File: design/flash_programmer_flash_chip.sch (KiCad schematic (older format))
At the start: 12 parts

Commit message: Work in progress: Come up with untested A9_P circuit
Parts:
- added Q? (x3): 2N3904, symbol Q_NPN_BCE
- added R? (x2): 1k, Resistors_SMD:R_0805_HandSoldering, symbol R
- added R?: 10k, Resistors_SMD:R_0805_HandSoldering, symbol R
- R?: value 10k -> 1k
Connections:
- wire segments 67 -> 80
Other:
- note added: "Logical NOT on the STU line"
- note added: "TODO: Test this A9_P circuit"
- note removed: "TODO: VPP needs to be disconnected somehow when not in write mode"
- moved on the sheet: D?, R?
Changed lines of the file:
@@
 Text Label 1400 1700 1    60   ~ 0
 A[0..16]
-Text Label 7150 4750 1    60   ~ 0
+Text Label 8150 6150 2    60   ~ 0
 A[0..16]
 Wire Wire Line
@@
 L GND #PWR?
 U 1 1 58BA7CFB
-P 9800 3050
-F 0 "#PWR?" H 9800 2800 50  0001 C CNN
-F 1 "GND" H 9800 2900 50  0000 C CNN
-F 2 "" H 9800 3050 50  0000 C CNN
-F 3 "" H 9800 3050 50  0000 C CNN
-	1    9800 3050
-	0    -1   -1   0
+P 6900 5500
+F 0 "#PWR?" H 6900 5250 50  0001 C CNN
+F 1 "GND" H 6900 5350 50  0000 C CNN
+F 2 "" H 6900 5500 50  0000 C CNN
+F 3 "" H 6900 5500 50  0000 C CNN
+	1    6900 5500
+	1    0    0    -1
 $EndComp
 $Comp
@@
 L R R?
 U 1 1 58BA7EA3
-P 3050 6200
-F 0 "R?" V 3130 6200 50  0000 C CNN
-F 1 "10k" V 3050 6200 50  0000 C CNN
-F 2 "Resistors_SMD:R_0805_HandSoldering" V 2980 6200 50  0001 C CNN
-F 3 "" H 3050 6200 50  0000 C CNN
-	1    3050 6200
-	-1   0    0    1
+P 6300 5200
+F 0 "R?" V 6380 5200 50  0000 C CNN
+F 1 "1k" V 6300 5200 50  0000 C CNN
+F 2 "Resistors_SMD:R_0805_HandSoldering" V 6230 5200 50  0001 C CNN
+F 3 "" H 6300 5200 50  0000 C CNN
+	1    6300 5200
+	0    -1   -1   0
 $EndComp
 Wire Wire Line
@@
 L D_Schottky D?
 U 1 1 58BAFC52
-P 6400 5050
-F 0 "D?" H 6400 5150 50  0000 C CNN
-F 1 "BAT54" H 6400 4950 50  0000 C CNN
-F 2 "" H 6400 5050 50  0000 C CNN
-F 3 "" H 6400 5050 50  0000 C CNN
-	1    6400 5050
-	1    0    0    -1
+P 7750 5400
+F 0 "D?" H 7750 5500 50  0000 C CNN
+F 1 "BAT54" H 7750 5300 50  0000 C CNN
+F 2 "" H 7750 5400 50  0000 C CNN
+F 3 "" H 7750 5400 50  0000 C CNN
+	1    7750 5400
+	0    1    1    0
 $EndComp
 Wire Bus Line
-	7150 5050 7150 4350
-Wire Wire Line
-	7150 5050 6550 5050
-Text Label 6750 5050 0    60   ~ 0
+	8450 6150 7750 6150
+Wire Wire Line
+	7750 5550 7750 6150
+Text Label 7750 5950 1    60   ~ 0
 A9
-Wire Wire Line
-	5400 5050 6250 5050
-Wire Wire Line
-	7150 5350 5900 5350
-Text Label 6750 5350 0    60   ~ 0
-VPP
-Wire Wire Line
-	5900 5350 5900 5050
-Connection ~ 5900 5050
-Text Label 5500 5050 0    60   ~ 0
-A9_P
 Wire Wire Line
 	3050 2400 3450 2400
 Text Label 3150 2400 0    60   ~ 0
 A9_P
-Text Notes 5150 5550 0    60   ~ 0
-TODO: VPP needs to be disconnected somehow when not in write mode
 Wire Wire Line
 	5100 7600 6350 7600
@@
 Text Label 5250 7600 0    60   ~ 0
 STU
+$Comp
+L Q_NPN_BCE Q?
+U 1 1 58BEF822
+P 6800 5200
+F 0 "Q?" H 7000 5250 50  0000 L CNN
+F 1 "2N3904" H 7000 5150 50  0000 L CNN
+F 2 "" H 7000 5300 50  0000 C CNN
+F 3 "" H 6800 5200 50  0000 C CNN
+	1    6800 5200
+	1    0    0    -1
+$EndComp
+Wire Wire Line
+	7750 4850 7750 5250
+Wire Wire Line
+	7750 5000 8300 5000
+Text Label 8100 5000 0    60   ~ 0
+A9_P
+Wire Wire Line
+	7350 4650 7450 4650
+Wire Wire Line
+	7050 4650 6900 4650
+Wire Wire Line
+	6900 4200 6900 5000
+Wire Wire Line
+	6900 4200 7750 4200
+Wire Wire Line
+	7750 4200 7750 4450
+Text Label 7300 4000 1    60   ~ 0
+VPP
+Wire Wire Line
+	7300 4200 7300 3800
+Connection ~ 7300 4200
+Connection ~ 6900 4650
+Wire Wire Line
+	6900 5400 6900 5500
+$Comp
+L Q_NPN_BCE Q?
+U 1 1 58BF03A4
+P 7650 4650
+F 0 "Q?" H 7850 4700 50  0000 L CNN
+F 1 "2N3904" H 7850 4600 50  0000 L CNN
+F 2 "" H 7850 4750 50  0000 C CNN
+F 3 "" H 7650 4650 50  0000 C CNN
+	1    7650 4650
+	1    0    0    -1
+$EndComp
+$Comp
+L R R?
+U 1 1 58BF0471
+P 7200 4650
+F 0 "R?" V 7280 4650 50  0000 C CNN
+F 1 "1k" V 7200 4650 50  0000 C CNN
+F 2 "Resistors_SMD:R_0805_HandSoldering" V 7130 4650 50  0001 C CNN
+F 3 "" H 7200 4650 50  0000 C CNN
+	1    7200 4650
+	0    -1   -1   0
+$EndComp
+Wire Wire Line
+	6450 5200 6600 5200
+$Comp
+L Q_NPN_BCE Q?
+U 1 1 58BF0576
+P 5750 5500
+F 0 "Q?" H 5950 5550 50  0000 L CNN
+F 1 "2N3904" H 5950 5450 50  0000 L CNN
+F 2 "" H 5950 5600 50  0000 C CNN
+F 3 "" H 5750 5500 50  0000 C CNN
+	1    5750 5500
+	1    0    0    -1
+$EndComp
+$Comp
+L GND #PWR?
+U 1 1 58BF059E
+P 5850 5800
+F 0 "#PWR?" H 5850 5550 50  0001 C CNN
+F 1 "GND" H 5850 5650 50  0000 C CNN
+F 2 "" H 5850 5800 50  0000 C CNN
+F 3 "" H 5850 5800 50  0000 C CNN
+	1    5850 5800
+	1    0    0    -1
+$EndComp
+Wire Wire Line
+	5850 5050 5850 5300
+Wire Wire Line
+	5850 5200 6150 5200
+Wire Wire Line
+	5850 5700 5850 5800
+$Comp
+L R R?
+U 1 1 58BF0846
+P 5850 4900
+F 0 "R?" V 5930 4900 50  0000 C CNN
+F 1 "10k" V 5850 4900 50  0000 C CNN
+F 2 "Resistors_SMD:R_0805_HandSoldering" V 5780 4900 50  0001 C CNN
+F 3 "" H 5850 4900 50  0000 C CNN
+	1    5850 4900
+	1    0    0    -1
+$EndComp
+Connection ~ 5850 5200
+$Comp
+L VCC #PWR?
+U 1 1 58BF0A83
+P 5850 4600
+F 0 "#PWR?" H 5850 4450 50  0001 C CNN
+F 1 "VCC" H 5850 4750 50  0000 C CNN
+F 2 "" H 5850 4600 50  0000 C CNN
+F 3 "" H 5850 4600 50  0000 C CNN
+	1    5850 4600
+	1    0    0    -1
+$EndComp
+Wire Wire Line
+	5850 4600 5850 4750
+Wire Wire Line
+	5550 5500 5350 5500
+$Comp
+L R R?
+U 1 1 58BF0CDC
+P 5200 5500
+F 0 "R?" V 5280 5500 50  0000 C CNN
+F 1 "1k" V 5200 5500 50  0000 C CNN
+F 2 "Resistors_SMD:R_0805_HandSoldering" V 5130 5500 50  0001 C CNN
+F 3 "" H 5200 5500 50  0000 C CNN
+	1    5200 5500
+	0    -1   -1   0
+$EndComp
+Wire Wire Line
+	5050 5500 4750 5500
+Text Label 4750 5500 0    60   ~ 0
+STU
+Wire Notes Line
+	5000 4200 5000 6150
+Wire Notes Line
+	5000 6150 6100 6150
+Wire Notes Line
+	6100 6150 6100 4200
+Wire Notes Line
+	6100 4200 5000 4200
+Text Notes 4900 4150 0    60   ~ 0
+Logical NOT on the STU line
+Connection ~ 7750 5000
+Text Notes 5600 3700 0    60   ~ 0
+TODO: Test this A9_P circuit
 $EndSCHEMATC

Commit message: Redo the A9_P circuit with a P-channel MOSFET to avoid voltage drop
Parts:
- removed D?: BAT54, symbol D_Schottky
- removed Q? (x3): 2N3904, symbol Q_NPN_BCE
- removed R? (x3): 1k, Resistors_SMD:R_0805_HandSoldering, symbol R
- removed R?: 10k, Resistors_SMD:R_0805_HandSoldering, symbol R
- added D302: BAT54, symbol D_Schottky
- added Q301: 2N3904, symbol Q_NPN_BCE
- added Q302: BSS84, symbol Q_PMOS_DGS
- added R302, R303: 4.7k, Resistors_SMD:R_0805_HandSoldering, symbol R
- added R304: 10k, Resistors_SMD:R_0805_HandSoldering, symbol R
- gave numbers to parts that had none: 10
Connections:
- wire segments 80 -> 77
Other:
- note added: "Circuit to switch between VPP and A9 on the A9 pin of the GLS27SF010.\nWhen STU is HIGH, then VPP is 5V, the P-Channel MOSFET shuts off,\nand the PNP Transistor turns on which pulls A9_P to ground (since the diode\nis preventing current from flowing in that direction)."
- note removed: "Logical NOT on the STU line"
- note removed: "TODO: Test this A9_P circuit"

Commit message: Redraw schematic for clarity
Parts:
- removed D301: LED, LEDs:LED_0805, symbol LED
- removed R301: 150, Resistors_SMD:R_0805_HandSoldering, symbol R
- removed R302: 4.7k, Resistors_SMD:R_0805_HandSoldering, symbol R
- removed U301: GLS27SF010, Housings_DIP:DIP-32_W15.24mm, symbol GLS27SF010
- removed U302: 2N3906, TO_SOT_Packages_SMD:SOT-23_Handsoldering, symbol 2N3906
- added U401: GLS27SF010, symbol GLS27SF010
- C401: renamed from C301; value 120nF -> 100nF
- renumbered C305 to C402, C302 to C403, C303 to C404, C304 to C405, D302 to D401, Q302 to Q401, Q301 to Q402, R304 to R401, R303 to R402, U303 to U402
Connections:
- net labels added: CE_L, OE_L, PGM_L
- net labels removed: CE#, OE#, PGM#
- wire segments 77 -> 67
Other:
- note added: "Bypass capacitor for GLS27SF010"
- note added: "Bypass capacitor for MAX662A"
- note removed: "Bypass capacitors for GLS27SF010"
- note removed: "Bypass capacitors for MAX662A"
- note removed: "Write indicator light"
- moved on the sheet: C401, C402, C403, C404, C405, D401, Q402, R401, R402, U402

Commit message: Associate footprints and correct pin orders for transistors
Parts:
- removed Q401: BSS84, symbol Q_PMOS_DGS
- removed Q402: 2N3904, symbol Q_NPN_BCE
- added Q401: BSS84P, TO_SOT_Packages_SMD:SOT-23_Handsoldering, symbol Q_PMOS_GSD
- added Q402: 2N3904, symbol Q_NPN_BEC
- D401: footprint (none) -> Diodes_SMD:D_SOT-23_ANK
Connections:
- wire segments 67 -> 73
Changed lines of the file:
@@
 $EndComp
 $Comp
-L GND #PWR041
+L GND #PWR404
 U 1 1 58BA7A65
 P 6100 7200
-F 0 "#PWR041" H 6100 6950 50  0001 C CNN
+F 0 "#PWR404" H 6100 6950 50  0001 C CNN
 F 1 "GND" H 6100 7050 50  0000 C CNN
 F 2 "" H 6100 7200 50  0000 C CNN
@@
 $EndComp
 $Comp
-L VCC #PWR042
+L VCC #PWR403
 U 1 1 58BA7A6B
 P 6100 6600
-F 0 "#PWR042" H 6100 6450 50  0001 C CNN
+F 0 "#PWR403" H 6100 6450 50  0001 C CNN
 F 1 "VCC" H 6100 6750 50  0000 C CNN
 F 2 "" H 6100 6600 50  0000 C CNN
@@
 	2550 6450 2750 6450
 $Comp
-L VCC #PWR043
+L VCC #PWR402
 U 1 1 58BA7A7D
 P 2800 5900
-F 0 "#PWR043" H 2800 5750 50  0001 C CNN
+F 0 "#PWR402" H 2800 5750 50  0001 C CNN
 F 1 "VCC" H 2800 6050 50  0000 C CNN
 F 2 "" H 2800 5900 50  0000 C CNN
@@
 $EndComp
 $Comp
-L GND #PWR044
+L GND #PWR401
 U 1 1 58BA7A83
 P 2550 5900
-F 0 "#PWR044" H 2550 5650 50  0001 C CNN
+F 0 "#PWR401" H 2550 5650 50  0001 C CNN
 F 1 "GND" H 2550 5750 50  0000 C CNN
 F 2 "" H 2550 5900 50  0000 C CNN
@@
 	9950 4500 9950 4650
 Wire Wire Line
-	7950 4850 9050 4850
-$Comp
-L GND #PWR045
+	7950 4850 8550 4850
+Wire Wire Line
+	8550 4850 9050 4850
+$Comp
+L GND #PWR407
 U 1 1 58BA7CE6
 P 8900 4750
-F 0 "#PWR045" H 8900 4500 50  0001 C CNN
+F 0 "#PWR407" H 8900 4500 50  0001 C CNN
 F 1 "GND" H 8900 4600 50  0000 C CNN
 F 2 "" H 8900 4750 50  0000 C CNN
@@
 $EndComp
 $Comp
-L VCC #PWR046
+L VCC #PWR408
 U 1 1 58BA7CEC
 P 8950 5100
-F 0 "#PWR046" H 8950 4950 50  0001 C CNN
+F 0 "#PWR408" H 8950 4950 50  0001 C CNN
 F 1 "VCC" H 8950 5250 50  0000 C CNN
 F 2 "" H 8950 5100 50  0000 C CNN
@@
 $EndComp
 $Comp
-L VCC #PWR047
+L VCC #PWR409
 U 1 1 58BA7D01
 P 10900 4500
-F 0 "#PWR047" H 10900 4350 50  0001 C CNN
+F 0 "#PWR409" H 10900 4350 50  0001 C CNN
 F 1 "VCC" H 10900 4650 50  0000 C CNN
 F 2 "" H 10900 4500 50  0000 C CNN
@@
 	8550 5300 8550 5400
 $Comp
-L GND #PWR048
+L GND #PWR406
 U 1 1 58BA7D27
 P 8550 5400
-F 0 "#PWR048" H 8550 5150 50  0001 C CNN
+F 0 "#PWR406" H 8550 5150 50  0001 C CNN
 F 1 "GND" H 8550 5250 50  0000 C CNN
 F 2 "" H 8550 5400 50  0000 C CNN
@@
 OE_L
 Wire Wire Line
-	7750 5150 6350 5150
-$Comp
-L Q_PMOS_DGS Q401
-U 1 1 58C18892
-P 6150 5150
-F 0 "Q401" H 6350 5200 50  0000 L CNN
-F 1 "BSS84" H 6350 5100 50  0000 L CNN
-F 2 "" H 6350 5250 50  0000 C CNN
-F 3 "" H 6150 5150 50  0000 C CNN
-	1    6150 5150
-	-1   0    0    -1
-$EndComp
-$Comp
-L Q_NPN_BCE Q402
-U 1 1 58C18984
-P 6750 4450
-F 0 "Q402" V 7000 4400 50  0000 L CNN
-F 1 "2N3904" V 6700 4550 50  0000 L CNN
-F 2 "" H 6950 4550 50  0000 C CNN
-F 3 "" H 6750 4450 50  0000 C CNN
-	1    6750 4450
-	0    -1   -1   0
-$EndComp
+	7750 5150 6750 5150
+Wire Wire Line
+	6750 5150 6350 5150
 $Comp
 L R R401
@@
 $EndComp
 Wire Wire Line
-	2100 4350 6150 4350
+	2100 4350 6050 4350
+Wire Wire Line
+	6050 4350 6150 4350
 Wire Wire Line
 	6550 4350 6450 4350
@@
 	6750 4750 6750 4650
 $Comp
-L GND #PWR049
+L GND #PWR405
 U 1 1 58C19559
 P 7050 4350
-F 0 "#PWR049" H 7050 4100 50  0001 C CNN
+F 0 "#PWR405" H 7050 4100 50  0001 C CNN
 F 1 "GND" H 7050 4200 50  0000 C CNN
 F 2 "" H 7050 4350 50  0000 C CNN
@@
 	6050 5350 6050 5550
 Wire Wire Line
-	2450 5550 7950 5550
+	2450 5550 6050 5550
+Wire Wire Line
+	6050 5550 7950 5550
 Text Label 6900 5550 0    60   ~ 0
 VPP
@@
 F 0 "D401" H 5200 3750 50  0000 C CNN
 F 1 "BAT54" H 5200 3550 50  0000 C CNN
-F 2 "" H 5200 3650 50  0000 C CNN
+F 2 "Diodes_SMD:D_SOT-23_ANK" H 5200 3650 50  0001 C CNN
 F 3 "" H 5200 3650 50  0000 C CNN
 	1    5200 3650
@@
 PGM_L
 $Comp
-L GND #PWR050
+L GND #PWR410
 U 1 1 58C1FD4A
 P 10900 5100
-F 0 "#PWR050" H 10900 4850 50  0001 C CNN
+F 0 "#PWR410" H 10900 4850 50  0001 C CNN
 F 1 "GND" H 10900 4950 50  0000 C CNN
 F 2 "" H 10900 5100 50  0000 C CNN
@@
 	8900 4750 9050 4750
 Wire Wire Line
-	7750 4400 7750 5150
+	7750 4400 7750 4650
+Wire Wire Line
+	7750 4650 7750 5150
 Connection ~ 7750 4650
 Wire Wire Line
@@
 	1500 2950 1250 2950
 Wire Bus Line
-	3050 1550 3050 3550
+	3050 1550 3050 1950
+Wire Bus Line
+	3050 1950 3050 2050
+Wire Bus Line
+	3050 2050 3050 2150
+Wire Bus Line
+	3050 2150 3050 2250
+Wire Bus Line
+	3050 2250 3050 2350
+Wire Bus Line
+	3050 2350 3050 2450
+Wire Bus Line
+	3050 2450 3050 2550
+Wire Bus Line
+	3050 2550 3050 2650
+Wire Bus Line
+	3050 2650 3050 2750
+Wire Bus Line
+	3050 2750 3050 2850
+Wire Bus Line
+	3050 2850 3050 2950
+Wire Bus Line
+	3050 2950 3050 3050
+Wire Bus Line
+	3050 3050 3050 3150
+Wire Bus Line
+	3050 3150 3050 3250
+Wire Bus Line
+	3050 3250 3050 3350
+Wire Bus Line
+	3050 3350 3050 3450
+Wire Bus Line
+	3050 3450 3050 3550
 Wire Bus Line
 	3050 1550 3150 1550
@@
 	2950 1950 3050 2050
 Wire Bus Line
-	1150 1550 1150 2850
+	1150 1550 1150 2150
+Wire Bus Line
+	1150 2150 1150 2250
+Wire Bus Line
+	1150 2250 1150 2350
+Wire Bus Line
+	1150 2350 1150 2450
+Wire Bus Line
+	1150 2450 1150 2550
+Wire Bus Line
+	1150 2550 1150 2650
+Wire Bus Line
+	1150 2650 1150 2750
+Wire Bus Line
+	1150 2750 1150 2850
 Wire Bus Line
 	1150 1550 1050 1550
@@
 	5350 3650 6050 3650
 Wire Wire Line
-	6050 3650 6050 4950
+	6050 3650 6050 4350
+Wire Wire Line
+	6050 4350 6050 4950
 Wire Wire Line
 	2100 4350 2100 3850
 Connection ~ 6050 5550
+$Comp
+L Q_PMOS_GSD Q401
+U 1 1 58C2CBBF
+P 6150 5150
+F 0 "Q401" H 6350 5200 50  0000 L CNN
+F 1 "BSS84P" H 6350 5100 50  0000 L CNN
+F 2 "TO_SOT_Packages_SMD:SOT-23_Handsoldering" H 6350 5250 50  0001 C CNN
+F 3 "" H 6150 5150 50  0000 C CNN
+	1    6150 5150
+	-1   0    0    -1
+$EndComp
+$Comp
+L Q_NPN_BEC Q402
+U 1 1 58C2EB64
+P 6750 4450
+F 0 "Q402" V 6700 4150 50  0000 L CNN
+F 1 "2N3904" V 6950 4300 50  0000 L CNN
+F 2 "" H 6950 4550 50  0000 C CNN
+F 3 "" H 6750 4450 50  0000 C CNN
+	1    6750 4450
+	0    -1   -1   0
+$EndComp
 $EndSCHEMATC

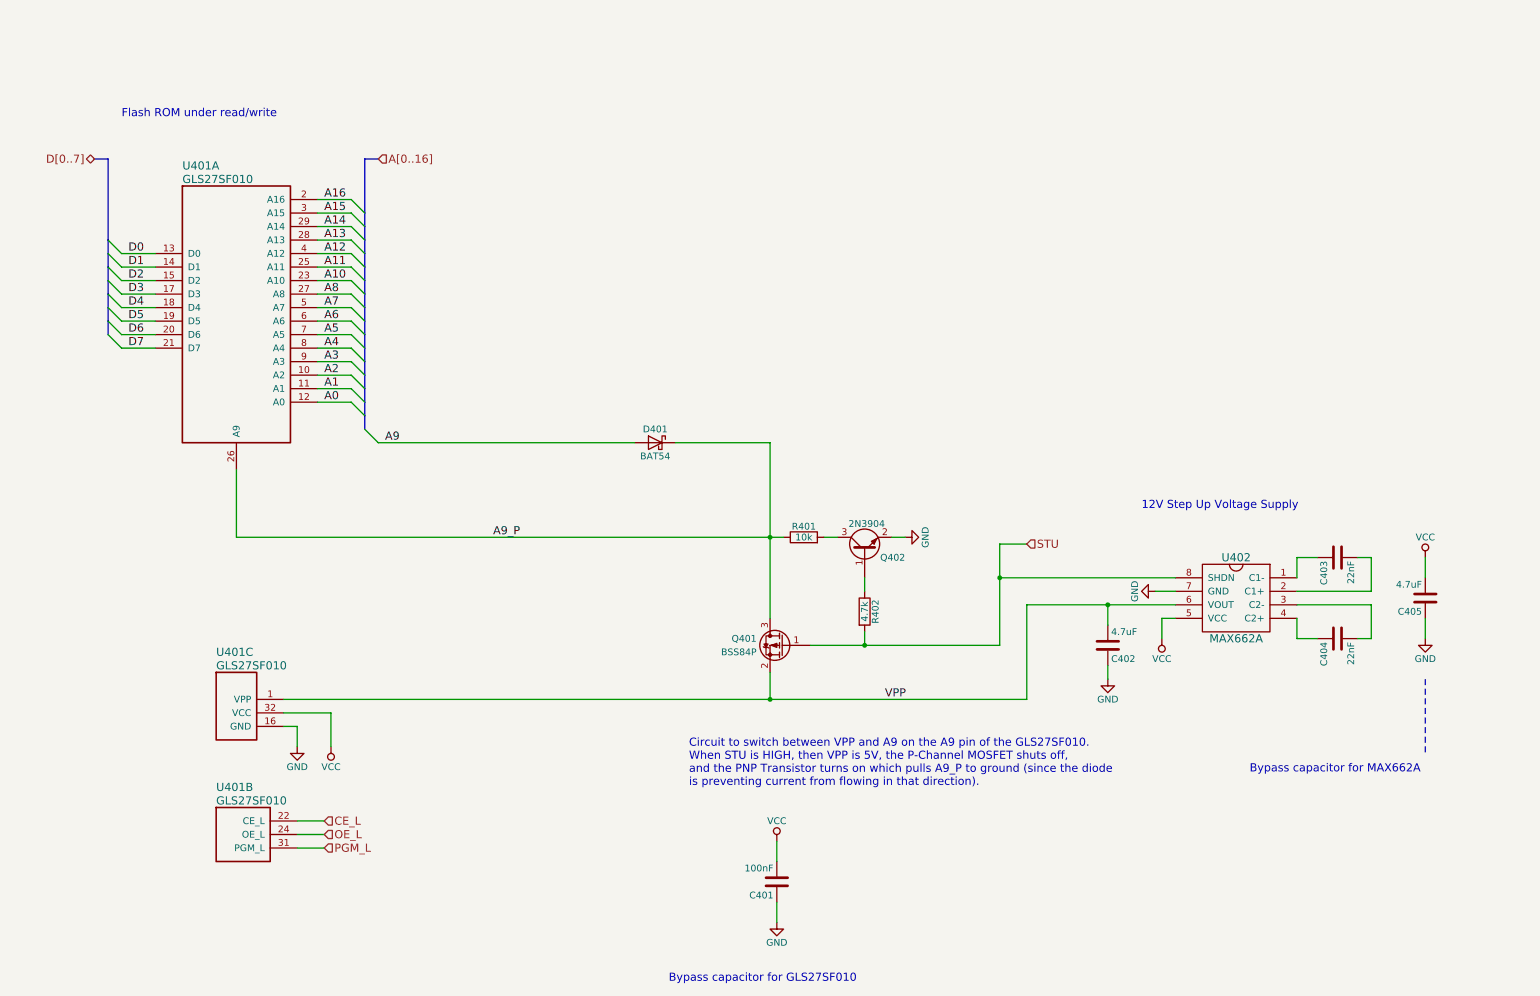
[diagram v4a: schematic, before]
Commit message: Bug fix and more schematic cleanup
The A9_VPP circuit wouldn't work in all cases, so I completely redid it and
it's simpler now.

Also started splitting up the schematic into even more sheets, and sprinkled in
some TODO comments.
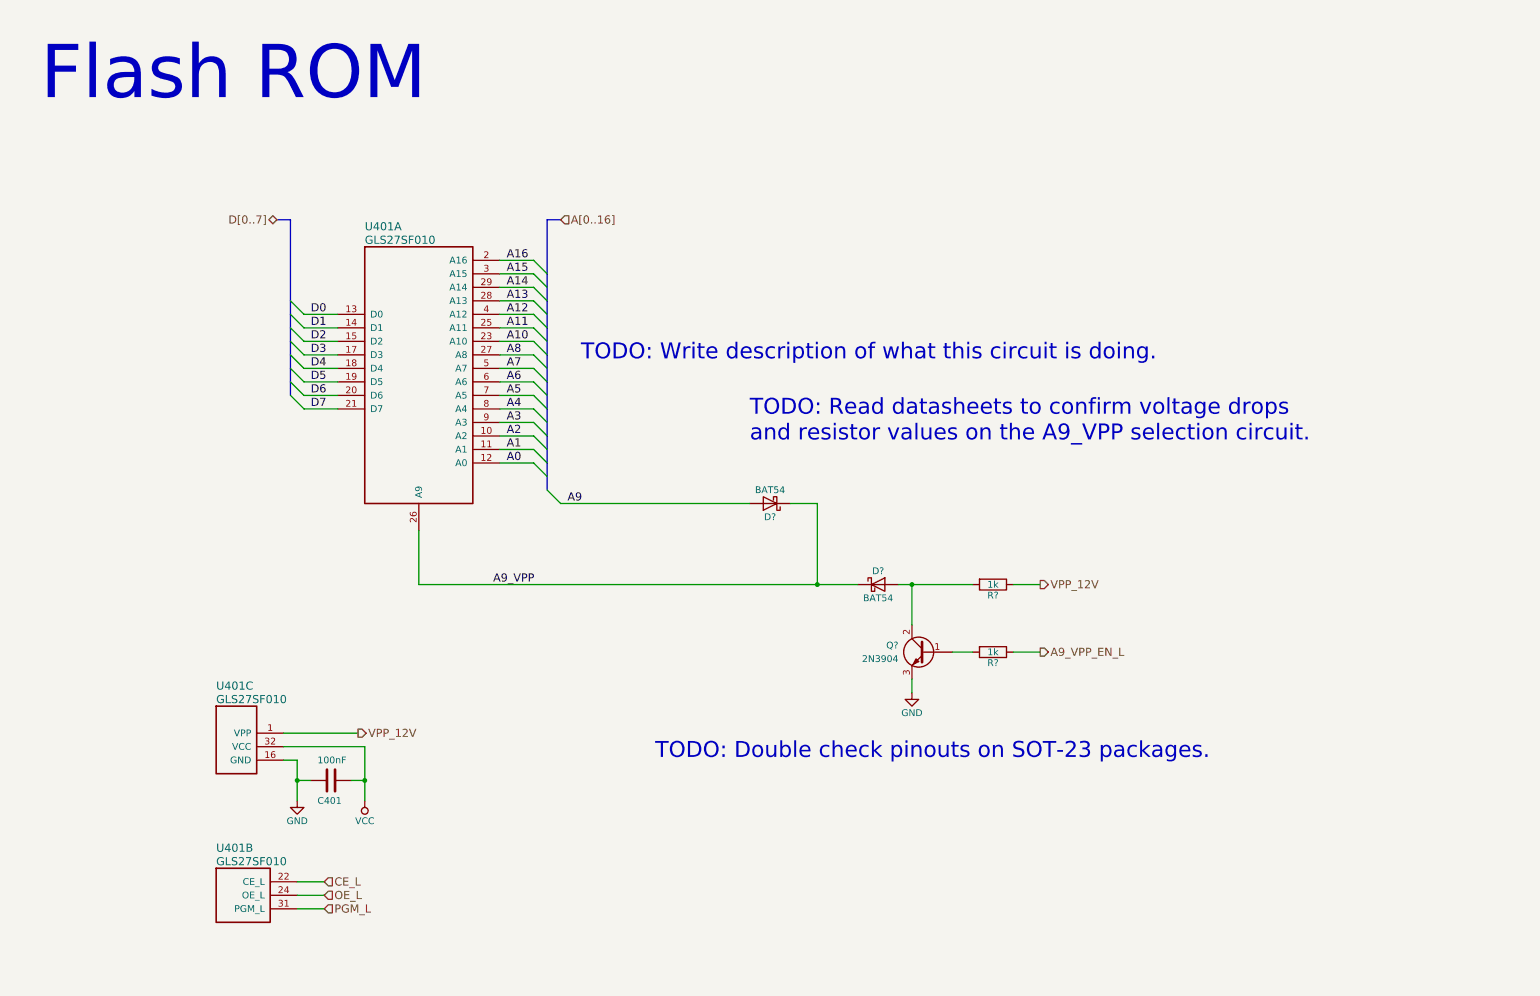
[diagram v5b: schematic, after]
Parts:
- removed C402, C405: 4.7uF, Capacitors_SMD:C_0805_HandSoldering, symbol C
- removed C403, C404: 22nF, Capacitors_SMD:C_0805_HandSoldering, symbol C
- removed D401: BAT54, Diodes_SMD:D_SOT-23_ANK, symbol D_Schottky
- removed Q401: BSS84P, TO_SOT_Packages_SMD:SOT-23_Handsoldering, symbol Q_PMOS_GSD
- removed Q402: 2N3904, symbol Q_NPN_BEC
- removed R401: 10k, Resistors_SMD:R_0805_HandSoldering, symbol R
- removed R402: 4.7k, Resistors_SMD:R_0805_HandSoldering, symbol R
- removed U402: MAX662A, Housings_SOIC:SOIC-8_3.9x4.9mm_Pitch1.27mm, symbol MAX662A
- added D? (x2): BAT54, symbol D_Schottky
- added Q?: 2N3904, symbol Q_NPN_BCE
- added R? (x2): 1k, symbol R
- C401: footprint Capacitors_SMD:C_0805_HandSoldering -> Resistors_SMD:R_0805_HandSoldering
- U401: footprint (none) -> Housings_DIP:DIP-32_W15.24mm
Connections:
- net A9: now also D?.2 (A)
- net GND: now also C401.2, Q?.3 (E); no longer C401.1
- net VCC: now also C401.1; no longer C401.2
- net A9_P renamed A9_VPP
- net A9_VPP: now also D?.1 (K), D?.1 (K)
- net VPP renamed VPP_12V
- net VPP_12V: now also R?.1
- new net: Q?.1 (B), R?.2
- new net: D?.2 (A), Q?.2 (C), R?.2
- new net A9_VPP_EN_L: R?.1
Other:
- note added: "Flash ROM"
- note added: "TODO: Double check pinouts on SOT-23 packages."
- note added: "TODO: Read datasheets to confirm voltage drops\nand resistor values on the A9_VPP selection circuit."
- note added: "TODO: Write description of what this circuit is doing."
- note removed: "12V Step Up Voltage Supply"
- note removed: "Bypass capacitor for GLS27SF010"
- note removed: "Bypass capacitor for MAX662A"
- note removed: "Circuit to switch between VPP and A9 on the A9 pin of the GLS27SF010.\nWhen STU is HIGH, then VPP is 5V, the P-Channel MOSFET shuts off,\nand the PNP Transistor turns on which pulls A9_P to ground (since the diode\nis preventing current from flowing in that direction)."
- note removed: "Flash ROM under read/write"
- moved on the sheet: C401, U401A, U401B, U401C
